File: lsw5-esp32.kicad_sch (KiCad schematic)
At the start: 32 parts, among them J1 Conn_02x03_Odd_Even, J2 Conn_01x04_Pin, J3 USB4105-GF-A, J4 Conn_02x05_Odd_Even, J5 Conn_01x03, Q1 AO3407A, U1 ESP32-S3-WROOM-1U, U2 LD1117S33TR_SOT223, U3 SP3485EN

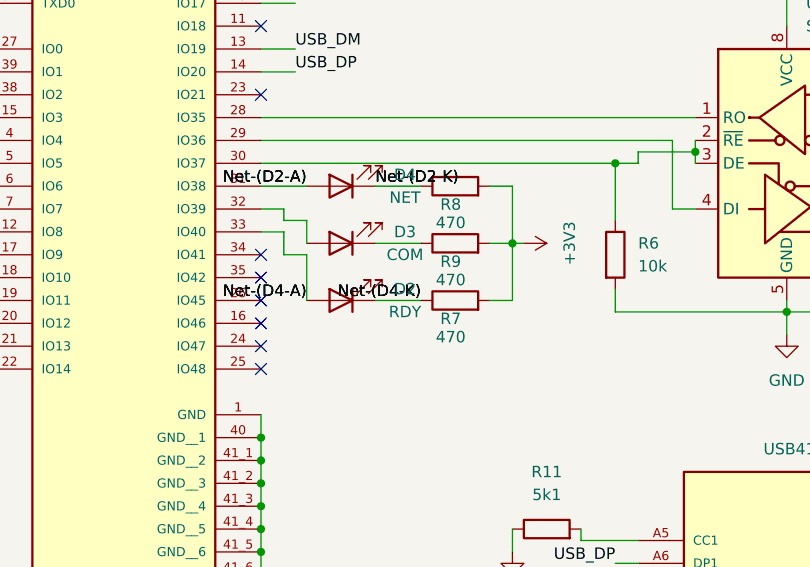
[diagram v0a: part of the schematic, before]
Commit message: Fix swapped LED labels
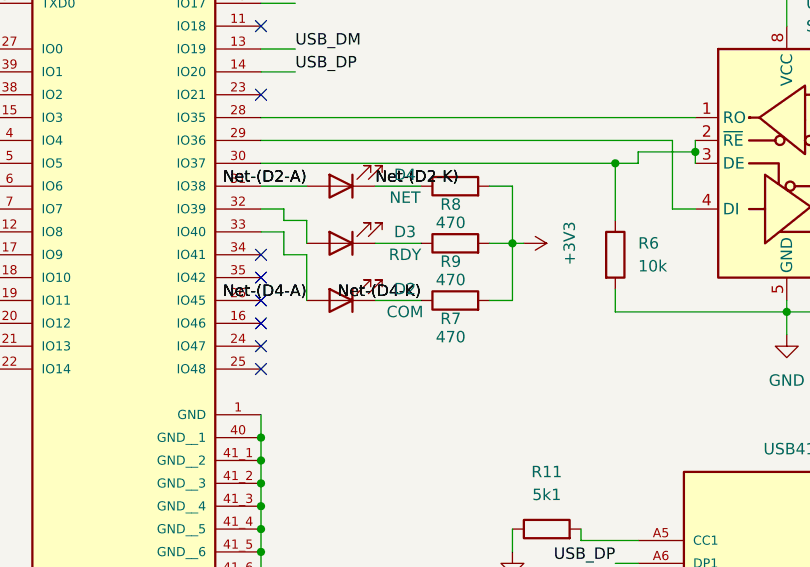
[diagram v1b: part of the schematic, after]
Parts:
- D2: value RDY -> COM
- D3: value COM -> RDY
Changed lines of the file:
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@@
 			)
 		)
-		(property "Value" "RDY"
+		(property "Value" "COM"
 			(at 90.932 90.17 0)
 			(effects
@@
 			)
 		)
-		(property "Value" "COM"
+		(property "Value" "RDY"
 			(at 90.932 83.82 0)
 			(effects

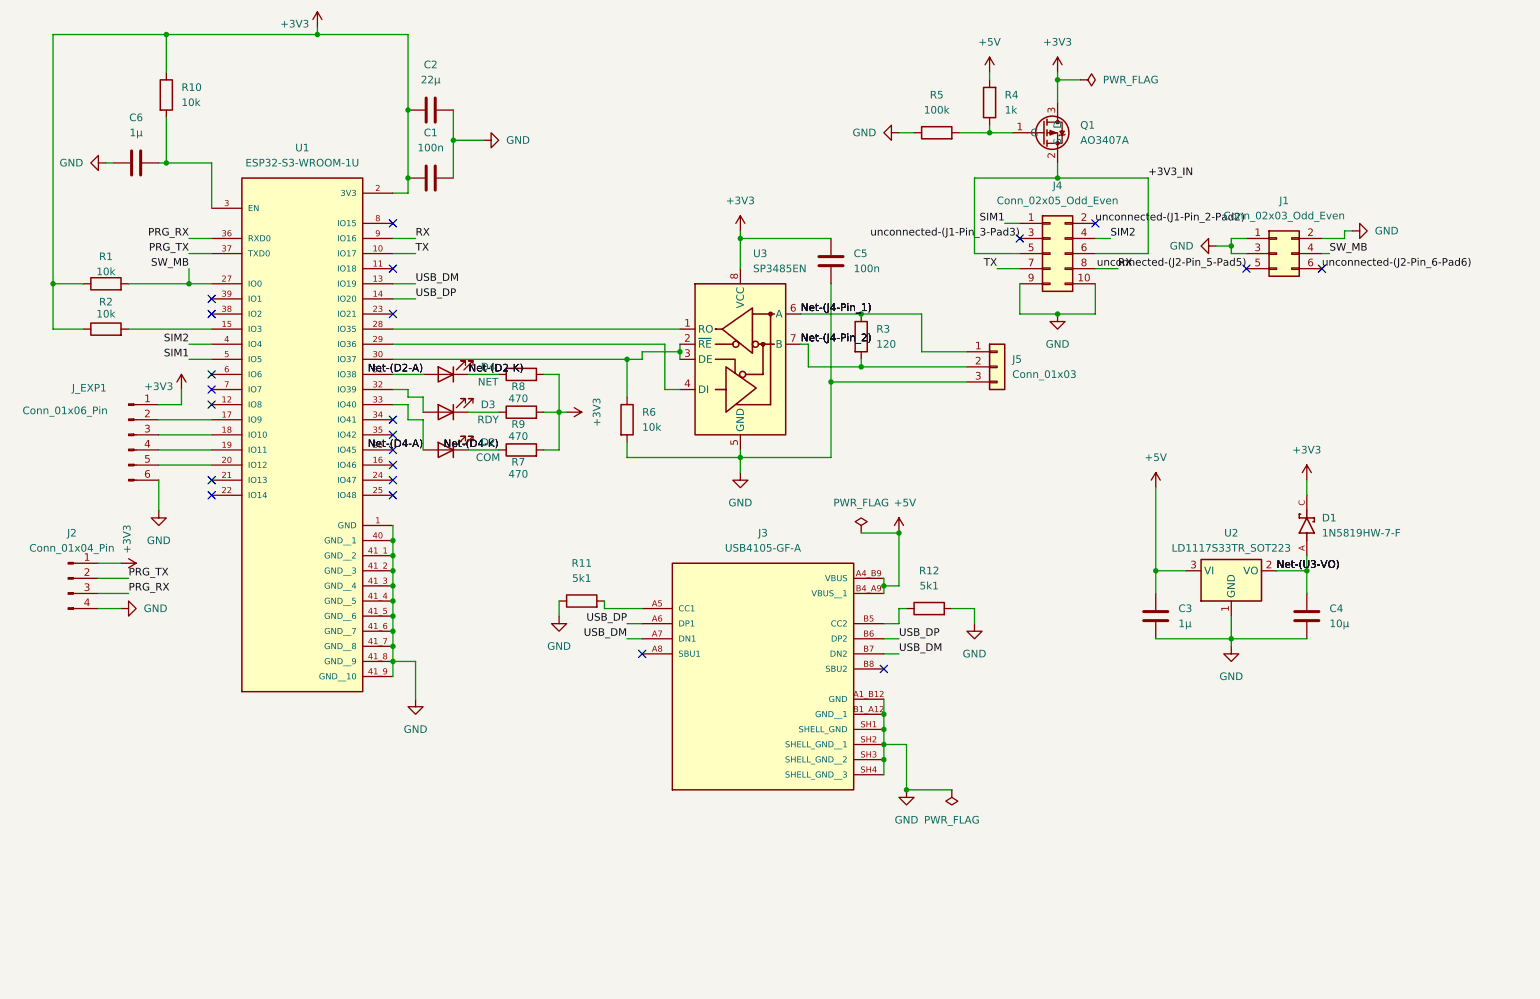
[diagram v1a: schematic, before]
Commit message: Move RS485 transceiver off octal SPI pins
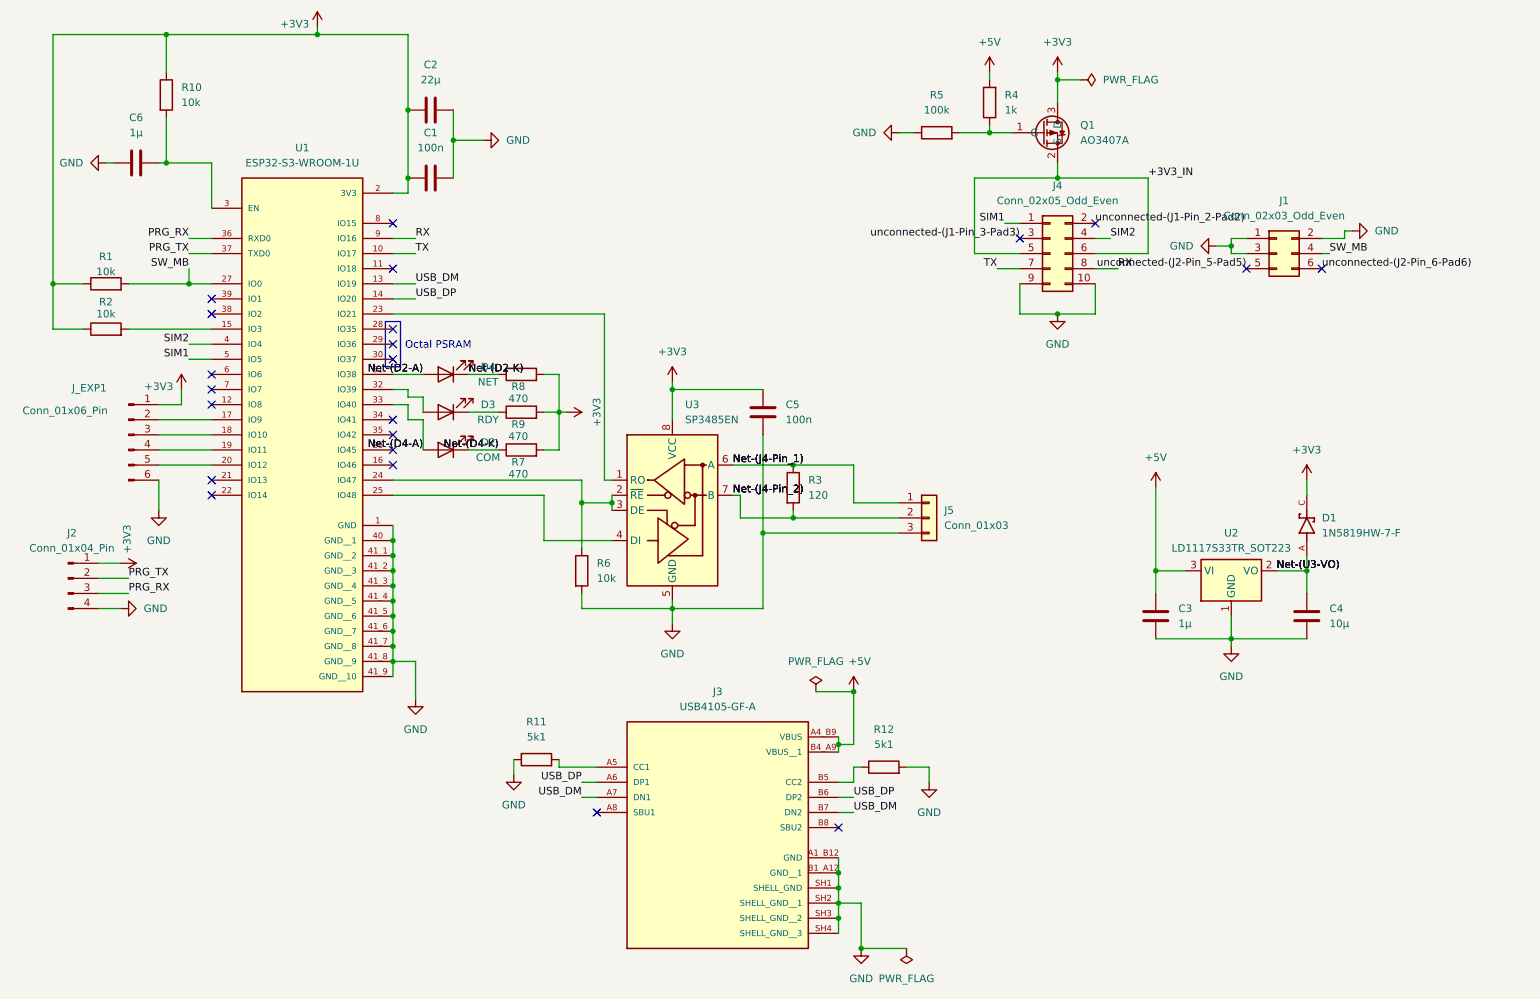
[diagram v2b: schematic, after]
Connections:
- net at R6.1, U3.2 (~{RE}), U3.3 (DE): now also U1.24 (IO47); no longer U1.30 (IO37)
- net at U3.1 (RO): now also U1.23 (IO21); no longer U1.28 (IO35)
- net at U3.4 (DI): now also U1.25 (IO48); no longer U1.29 (IO36)
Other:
- note added: "Octal PSRAM"
- moved on the sheet: C5, J3, J5, R11, R12, R3, R6, U3
